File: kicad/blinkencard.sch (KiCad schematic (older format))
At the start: 4 parts

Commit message: Use CP2102A USB-UART and GPIO instead of ESP32 to keep it simple. Add power section and start routing.
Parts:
- removed H1, H2, H3, H4: MountingHole_Pad, MountingHole:MountingHole_2.2mm_M2_Pad_Via, symbol Mechanical:MountingHole_Pad
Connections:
- net labels removed: GND
- wire segments 4 -> 0
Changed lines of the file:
@@
 $EndSheet
 $Sheet
-S 2350 5450 2650 2100
-U 5DF1D240
-F0 "wifi" 50
-F1 "blinkencard_wifi.sch" 50
+S 3650 4600 3300 1700
+U 5DDAD9CA
+F0 "usb_and_power" 50
+F1 "blinkencard_usb.sch" 50
 $EndSheet
-$Comp
-L Mechanical:MountingHole_Pad H4
-U 1 1 5DF7001B
-P 8600 5700
-F 0 "H4" H 8700 5749 50  0000 L CNN
-F 1 "MountingHole_Pad" H 8700 5658 50  0000 L CNN
-F 2 "MountingHole:MountingHole_2.2mm_M2_Pad_Via" H 8600 5700 50  0001 C CNN
-F 3 "~" H 8600 5700 50  0001 C CNN
-	1    8600 5700
-	1    0    0    -1
-$EndComp
-$Comp
-L Mechanical:MountingHole_Pad H3
-U 1 1 5DF703E7
-P 8400 5700
-F 0 "H3" H 8500 5749 50  0000 L CNN
-F 1 "MountingHole_Pad" H 8500 5658 50  0000 L CNN
-F 2 "MountingHole:MountingHole_2.2mm_M2_Pad_Via" H 8400 5700 50  0001 C CNN
-F 3 "~" H 8400 5700 50  0001 C CNN
-	1    8400 5700
-	1    0    0    -1
-$EndComp
-$Comp
-L Mechanical:MountingHole_Pad H2
-U 1 1 5DF7062A
-P 8200 5700
-F 0 "H2" H 8300 5749 50  0000 L CNN
-F 1 "MountingHole_Pad" H 8300 5658 50  0000 L CNN
-F 2 "MountingHole:MountingHole_2.2mm_M2_Pad_Via" H 8200 5700 50  0001 C CNN
-F 3 "~" H 8200 5700 50  0001 C CNN
-	1    8200 5700
-	1    0    0    -1
-$EndComp
-$Comp
-L Mechanical:MountingHole_Pad H1
-U 1 1 5DF70808
-P 8000 5700
-F 0 "H1" H 8100 5749 50  0000 L CNN
-F 1 "MountingHole_Pad" H 8100 5658 50  0000 L CNN
-F 2 "MountingHole:MountingHole_2.2mm_M2_Pad_Via" H 8000 5700 50  0001 C CNN
-F 3 "~" H 8000 5700 50  0001 C CNN
-	1    8000 5700
-	1    0    0    -1
-$EndComp
-$Comp
-L power:GND #PWR0101
-U 1 1 5DF70ADF
-P 8200 5900
-F 0 "#PWR0101" H 8200 5650 50  0001 C CNN
-F 1 "GND" H 8205 5727 50  0000 C CNN
-F 2 "" H 8200 5900 50  0001 C CNN
-F 3 "" H 8200 5900 50  0001 C CNN
-	1    8200 5900
-	1    0    0    -1
-$EndComp
-Wire Wire Line
-	8000 5800 8200 5800
-Wire Wire Line
-	8400 5800 8200 5800
-Connection ~ 8200 5800
-Wire Wire Line
-	8600 5800 8400 5800
-Connection ~ 8400 5800
-Wire Wire Line
-	8200 5800 8200 5900
 $EndSCHEMATC

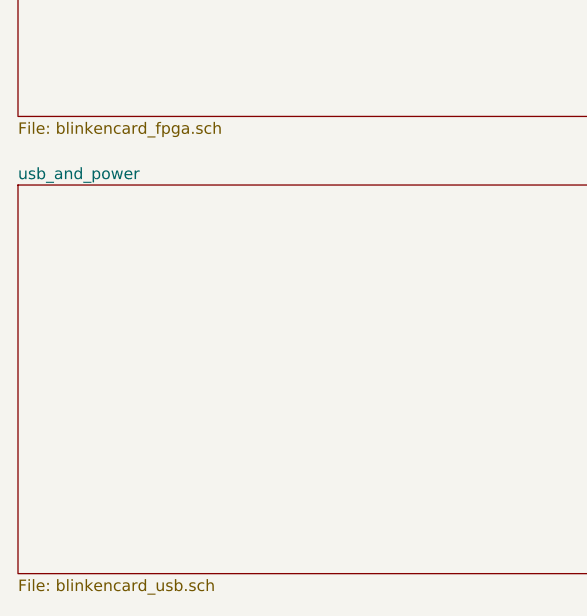
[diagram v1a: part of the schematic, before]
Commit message: Start v2.0 - change USB-UART to ESP32 and bugfixes
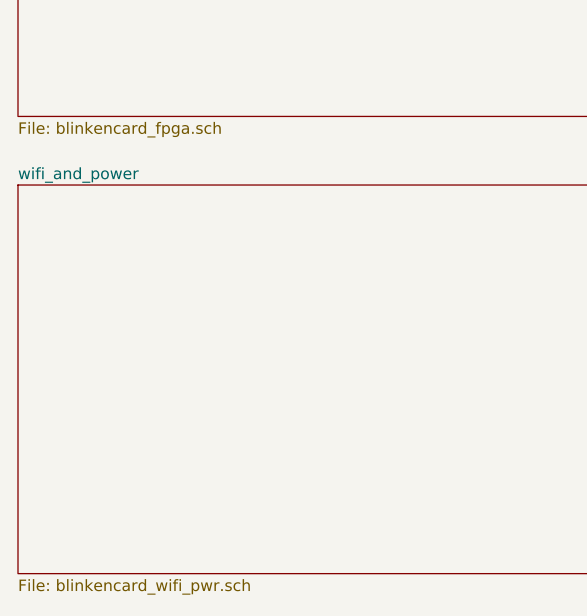
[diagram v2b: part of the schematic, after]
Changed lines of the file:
@@
 S 3650 4600 3300 1700
 U 5DDAD9CA
-F0 "usb_and_power" 50
-F1 "blinkencard_usb.sch" 50
+F0 "wifi_and_power" 50
+F1 "blinkencard_wifi_pwr.sch" 50
 $EndSheet
 $EndSCHEMATC
